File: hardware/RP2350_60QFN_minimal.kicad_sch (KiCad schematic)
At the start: 39 parts, among them J4 PinHeader_1x03, J5 4677, SW1 SW_Push, SW2 SW_Push, U1 RP2350_60QFN, U3 W25Q128JVS, Y1 ABM8-272-T3

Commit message: feat(hardware): Finish component layout
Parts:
- removed H4: MountingHole, MountingHole:MountingHole_2.7mm_M2.5, symbol Mechanical:MountingHole
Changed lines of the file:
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@@
-	)
-	(symbol
-		(lib_id "Mechanical:MountingHole")
-		(at 318.77 242.57 0)
-		(unit 1)
-		(exclude_from_sim no)
-		(in_bom yes)
-		(on_board yes)
-		(dnp no)
-		(property "Reference" "H4"
-			(at 321.31 241.4016 0)
-			(effects
-				(font
-					(size 1.27 1.27)
-				)
-				(justify left)
-			)
-		)
-		(property "Value" "MountingHole"
-			(at 321.31 243.713 0)
-			(effects
-				(font
-					(size 1.27 1.27)
-				)
-				(justify left)
-			)
-		)
-		(property "Footprint" "MountingHole:MountingHole_2.7mm_M2.5"
-			(at 318.77 242.57 0)
-			(effects
-				(font
-					(size 1.27 1.27)
-				)
-				(hide yes)
-			)
-		)
-		(property "Datasheet" "~"
-			(at 318.77 242.57 0)
-			(effects
-				(font
-					(size 1.27 1.27)
-				)
-				(hide yes)
-			)
-		)
-		(property "Description" ""
-			(at 318.77 242.57 0)
-			(effects
-				(font
-					(size 1.27 1.27)
-				)
-			)
-		)
-		(property "Purchase Link" ""
-			(at 318.77 242.57 0)
-			(effects
-				(font
-					(size 1.27 1.27)
-				)
-				(hide yes)
-			)
-		)
-		(instances
-			(project "RP2350_60QFN_minimal"
-				(path "/94683f5c-9cd9-448e-be96-9792537b5cb8"
-					(reference "H4")
-					(unit 1)
-				)
-			)
-		)
 	)
 	(symbol

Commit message: feat(hardware): updted design rules
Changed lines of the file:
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@@
 		)
 		(property "Value" "GND"
-			(at 102.87 198.12 0)
+			(at 106.68 200.66 0)
 			(effects
 				(font
@@
 			)
 		)
-		(property "Description" ""
+		(property "Description" "Power symbol creates a global label with name \"GND\" , ground"
 			(at 106.68 196.85 0)
 			(effects
@@
 					(size 1.27 1.27)
 				)
+				(hide yes)
 			)
 		)
@@
 		)
 		(property "Value" "GND"
-			(at 116.84 170.18 0)
+			(at 113.03 172.72 0)
 			(effects
 				(font
@@
 			)
 		)
-		(property "Description" ""
+		(property "Description" "Power symbol creates a global label with name \"GND\" , ground"
 			(at 113.03 168.91 0)
 			(effects
@@
 					(size 1.27 1.27)
 				)
+				(hide yes)
 			)
 		)
@@
 		)
 		(property "Value" "GND"
-			(at 236.347 221.5642 0)
+			(at 236.22 220.98 0)
 			(effects
 				(font
@@
 			)
 		)
-		(property "Description" ""
+		(property "Description" "Power symbol creates a global label with name \"GND\" , ground"
 			(at 236.22 217.17 0)
 			(effects
@@
 					(size 1.27 1.27)
 				)
+				(hide yes)
 			)
 		)
@@
 		)
 		(property "Value" "GND"
-			(at 353.06 146.05 0)
+			(at 356.87 148.59 0)
 			(effects
 				(font
@@
 			)
 		)
-		(property "Description" ""
+		(property "Description" "Power symbol creates a global label with name \"GND\" , ground"
 			(at 356.87 144.78 0)
 			(effects
@@
 					(size 1.27 1.27)
 				)
+				(hide yes)
 			)
 		)
@@
 		)
 		(property "Value" "GND"
-			(at 165.862 161.8742 0)
+			(at 165.735 161.29 0)
 			(effects
 				(font
@@
 			)
 		)
-		(property "Description" ""
+		(property "Description" "Power symbol creates a global label with name \"GND\" , ground"
 			(at 165.735 157.48 0)
 			(effects
@@
 					(size 1.27 1.27)
 				)
+				(hide yes)
 			)
 		)
@@
 		)
 		(property "Value" "GND"
-			(at 187.96 120.65 0)
+			(at 191.77 123.19 0)
 			(effects
 				(font
@@
 			)
 		)
-		(property "Description" ""
+		(property "Description" "Power symbol creates a global label with name \"GND\" , ground"
 			(at 191.77 119.38 0)
 			(effects
@@
 					(size 1.27 1.27)
 				)
+				(hide yes)
 			)
 		)
@@
 		)
 		(property "Value" "GND"
-			(at 208.407 64.0842 0)
+			(at 208.28 63.5 0)
 			(effects
 				(font
@@
 			)
 		)
-		(property "Description" ""
+		(property "Description" "Power symbol creates a global label with name \"GND\" , ground"
 			(at 208.28 59.69 0)
 			(effects
@@
 					(size 1.27 1.27)
 				)
+				(hide yes)
 			)
 		)
@@
 		)
 		(property "Value" "GND"
-			(at 240.03 53.34 0)
+			(at 236.22 55.88 0)
 			(effects
 				(font
@@
 			)
 		)
-		(property "Description" ""
+		(property "Description" "Power symbol creates a global label with name \"GND\" , ground"
 			(at 236.22 52.07 0)
 			(effects
@@
 					(size 1.27 1.27)
 				)
+				(hide yes)
 			)
 		)
@@
 		)
 		(property "Value" "GND"
-			(at 354.838 182.8292 0)
+			(at 354.965 182.245 0)
 			(effects
 				(font
@@
 			)
 		)
-		(property "Description" ""
+		(property "Description" "Power symbol creates a global label with name \"GND\" , ground"
 			(at 354.965 178.435 0)
 			(effects
@@
 					(size 1.27 1.27)
 				)
+				(hide yes)
 			)
 		)
@@
 		)
 		(property "Value" "GND"
-			(at 181.737 97.1042 0)
+			(at 181.61 96.52 0)
 			(effects
 				(font
@@
 			)
 		)
-		(property "Description" ""
+		(property "Description" "Power symbol creates a global label with name \"GND\" , ground"
 			(at 181.61 92.71 0)
 			(effects
@@
 					(size 1.27 1.27)
 				)
+				(hide yes)
 			)
 		)
@@
 	)
 	(symbol
-		(lib_name "GND_1")
 		(lib_id "power:GND")
 		(at 90.17 248.92 0)
@@
 		)
 		(property "Value" "GND"
-			(at 219.71 53.34 0)
+			(at 223.52 55.88 0)
 			(effects
 				(font
@@
 			)
 		)
-		(property "Description" ""
+		(property "Description" "Power symbol creates a global label with name \"GND\" , ground"
 			(at 223.52 52.07 0)
 			(effects
@@
 					(size 1.27 1.27)
 				)
+				(hide yes)
 			)
 		)
@@
 	)
 	(symbol
-		(lib_name "GND_3")
 		(lib_id "power:GND")
 		(at 340.36 92.71 0)
@@
 		)
 		(property "Value" "GND"
-			(at 326.263 97.7392 0)
+			(at 326.39 97.155 0)
 			(effects
 				(font
@@
 			)
 		)
-		(property "Description" ""
+		(property "Description" "Power symbol creates a global label with name \"GND\" , ground"
 			(at 326.39 93.345 0)
 			(effects
@@
 					(size 1.27 1.27)
 				)
+				(hide yes)
 			)
 		)
@@
 	)
 	(symbol
-		(lib_name "GND_4")
 		(lib_id "power:GND")
 		(at 320.04 166.37 0)
@@
 	)
 	(symbol
-		(lib_name "GND_2")
 		(lib_id "power:GND")
 		(at 138.43 228.6 0)
@@
 		)
 		(property "Value" "GND"
-			(at 148.59 189.23 0)
+			(at 152.4 191.77 0)
 			(effects
 				(font
@@
 			)
 		)
-		(property "Description" ""
+		(property "Description" "Power symbol creates a global label with name \"GND\" , ground"
 			(at 152.4 187.96 0)
 			(effects
@@
 					(size 1.27 1.27)
 				)
+				(hide yes)
 			)
 		)
@@
 		)
 		(property "Value" "GND"
-			(at 149.86 138.43 0)
+			(at 146.05 140.97 0)
 			(effects
 				(font
@@
 			)
 		)
-		(property "Description" ""
+		(property "Description" "Power symbol creates a global label with name \"GND\" , ground"
 			(at 146.05 137.16 0)
 			(effects
@@
 					(size 1.27 1.27)
 				)
+				(hide yes)
 			)
 		)

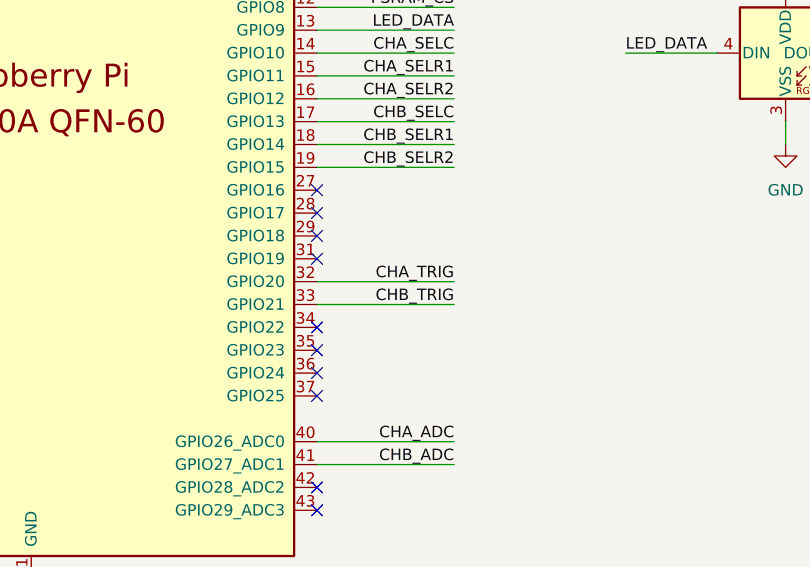
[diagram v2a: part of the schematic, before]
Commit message: feat(hardware): Connect bottom layer data lines
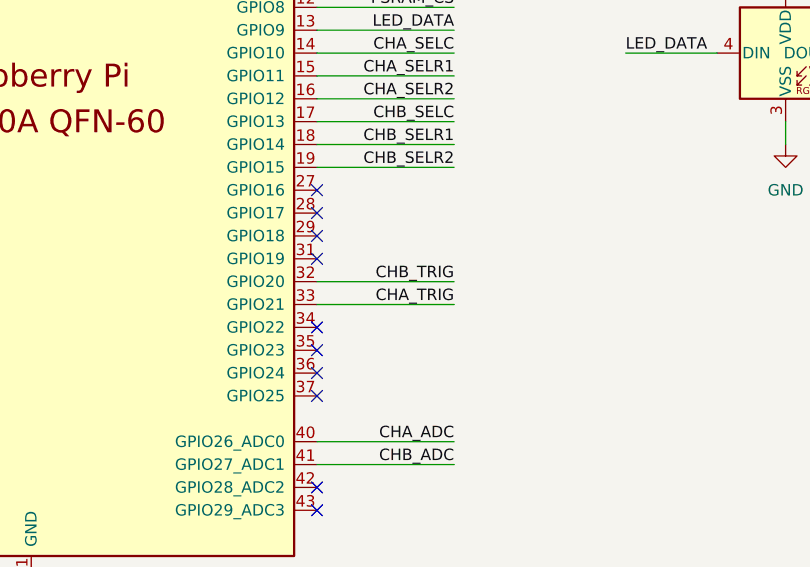
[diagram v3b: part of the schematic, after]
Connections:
- net CHA_TRIG: now also U1.33 (GPIO21); no longer U1.32 (GPIO20)
- net CHB_TRIG: now also U1.32 (GPIO20); no longer U1.33 (GPIO21)
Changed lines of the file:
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@@
 		)
 	)
-	(label "CHB_TRIG"
+	(label "CHA_TRIG"
 		(at 283.21 184.15 180)
 		(effects
@@
 		)
 	)
-	(label "CHA_TRIG"
+	(label "CHB_TRIG"
 		(at 283.21 181.61 180)
 		(effects

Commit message: fix(hardware): Fix neopixel footprint size
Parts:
- D5: footprint LED_SMD:LED_WS2812B_PLCC4_5.0x5.0mm_P3.2mm -> LED_SMD:LED_WS2812B-Mini_PLCC4_3.5x3.5mm
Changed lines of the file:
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@@
 			)
 		)
-		(property "Footprint" "LED_SMD:LED_WS2812B_PLCC4_5.0x5.0mm_P3.2mm"
+		(property "Footprint" "LED_SMD:LED_WS2812B-Mini_PLCC4_3.5x3.5mm"
 			(at 321.31 163.83 0)
 			(effects
